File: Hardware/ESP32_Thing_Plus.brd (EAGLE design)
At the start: 33 x 58.9 mm, 52 parts, among them Q1 2.5A/30V, Q2 MBT3904DW1T1, U1 MCP73831, U2 ESP-WROOM-32, U3 AP2112K-3.3V, U4 FT231XS

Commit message: Ready for qc review
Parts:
- added FD3, FD4: FIDUCIALUFIDUCIAL, SparkFun-Aesthetics:MICRO-FIDUCIAL
- moved FD2 94.5 mm to (31.8, 57.1), flipped to the top
- moved J2 63.5 mm to (31.8, 1.27), flipped to the top
- moved LOGO1 57.4 mm to (28.7, 12.7), flipped to the top
- moved D4 55.9 mm to (27.9, 29.2), flipped to the top
- moved R8 55.9 mm to (27.9, 27.7), flipped to the top
- moved LOGO3 54.6 mm to (27.3, 53.1), flipped to the bottom
- moved J3 52.1 mm to (26.0, 5.08), flipped to the top
- moved R9 43.2 mm to (21.6, 24.1), flipped to the top
- moved C19 41.9 mm to (21.0, 11.4), flipped to the top
- moved C6 38.1 mm to (19.1, 8.51), flipped to the top
- moved JP2 38.1 mm to (19.1, 5.97), flipped to the top
- moved R17 38.1 mm to (19.1, 19.1), flipped to the top
- moved S2 38.1 mm to (19.1, 24.1), flipped to the top
- moved R5 36.8 mm to (18.4, 14.6), flipped to the top
- moved R6 36.8 mm to (18.4, 14.6), flipped to the top
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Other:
- board text added: "Mike Hord"
- board text added: "Original ESP32 Thing Design by Jim Lindblom"
- board text removed: "Jim Lindblom"

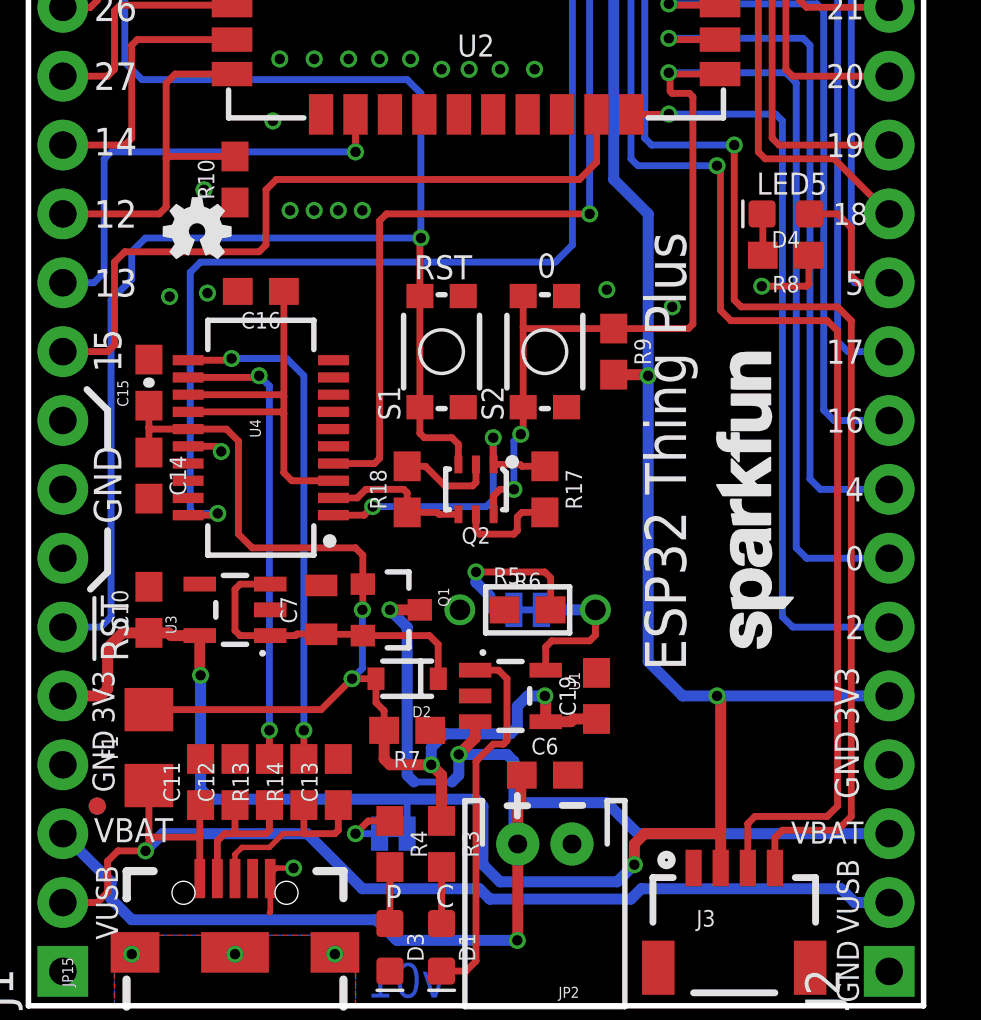
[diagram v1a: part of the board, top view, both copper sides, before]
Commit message: Revised per QC double check
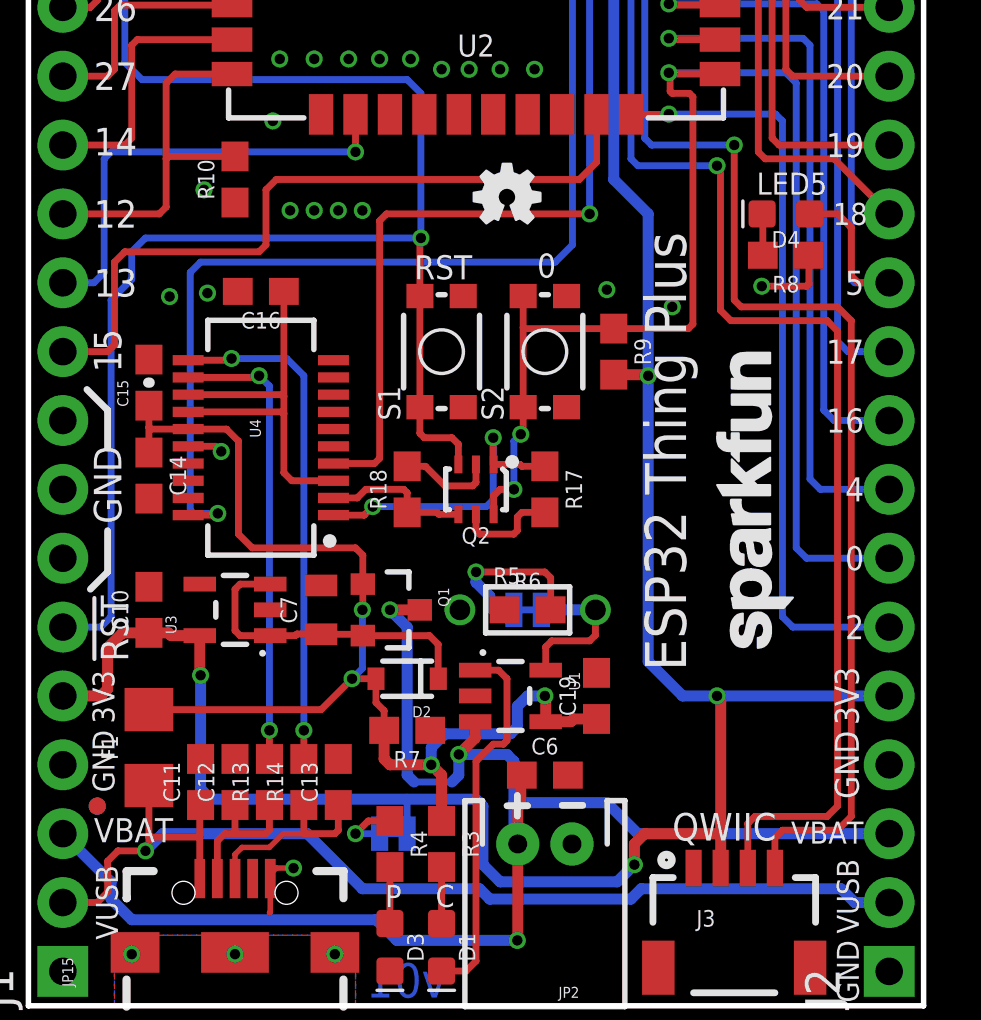
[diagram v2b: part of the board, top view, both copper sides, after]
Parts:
- moved LOGO2 11.5 mm to (17.7, 29.8)
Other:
- board text added: "Measurements in inches"
- board text added: "QWIIC"
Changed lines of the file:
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@@
 <layers>
 <layer number="1" name="Top" color="4" fill="1" visible="yes" active="yes"/>
-<layer number="2" name="Route2" color="1" fill="3" visible="no" active="yes"/>
-<layer number="15" name="Route15" color="4" fill="6" visible="no" active="yes"/>
+<layer number="2" name="Route2" color="1" fill="3" visible="yes" active="yes"/>
+<layer number="15" name="Route15" color="4" fill="6" visible="yes" active="yes"/>
 <layer number="16" name="Bottom" color="1" fill="1" visible="yes" active="yes"/>
 <layer number="17" name="Pads" color="2" fill="1" visible="yes" active="yes"/>
@@
 <layer number="23" name="tOrigins" color="15" fill="1" visible="yes" active="yes"/>
 <layer number="24" name="bOrigins" color="15" fill="1" visible="yes" active="yes"/>
-<layer number="25" name="tNames" color="7" fill="1" visible="no" active="yes"/>
-<layer number="26" name="bNames" color="7" fill="1" visible="no" active="yes"/>
-<layer number="27" name="tValues" color="7" fill="1" visible="no" active="yes"/>
-<layer number="28" name="bValues" color="7" fill="1" visible="no" active="yes"/>
-<layer number="29" name="tStop" color="7" fill="3" visible="no" active="yes"/>
-<layer number="30" name="bStop" color="7" fill="6" visible="no" active="yes"/>
-<layer number="31" name="tCream" color="7" fill="4" visible="no" active="yes"/>
-<layer number="32" name="bCream" color="7" fill="5" visible="no" active="yes"/>
-<layer number="39" name="tKeepout" color="4" fill="11" visible="no" active="yes"/>
-<layer number="40" name="bKeepout" color="1" fill="11" visible="no" active="yes"/>
-<layer number="41" name="tRestrict" color="4" fill="10" visible="no" active="yes"/>
-<layer number="42" name="bRestrict" color="1" fill="10" visible="no" active="yes"/>
-<layer number="43" name="vRestrict" color="2" fill="10" visible="no" active="yes"/>
-<layer number="44" name="Drills" color="7" fill="1" visible="no" active="yes"/>
+<layer number="25" name="tNames" color="7" fill="1" visible="yes" active="yes"/>
+<layer number="26" name="bNames" color="7" fill="1" visible="yes" active="yes"/>
+<layer number="27" name="tValues" color="7" fill="1" visible="yes" active="yes"/>
+<layer number="28" name="bValues" color="7" fill="1" visible="yes" active="yes"/>
+<layer number="29" name="tStop" color="7" fill="3" visible="yes" active="yes"/>
+<layer number="30" name="bStop" color="7" fill="6" visible="yes" active="yes"/>
+<layer number="31" name="tCream" color="7" fill="4" visible="yes" active="yes"/>
+<layer number="32" name="bCream" color="7" fill="5" visible="yes" active="yes"/>
+<layer number="39" name="tKeepout" color="4" fill="11" visible="yes" active="yes"/>
+<layer number="40" name="bKeepout" color="1" fill="11" visible="yes" active="yes"/>
+<layer number="41" name="tRestrict" color="4" fill="10" visible="yes" active="yes"/>
+<layer number="42" name="bRestrict" color="1" fill="10" visible="yes" active="yes"/>
+<layer number="43" name="vRestrict" color="2" fill="10" visible="yes" active="yes"/>
+<layer number="44" name="Drills" color="7" fill="1" visible="yes" active="yes"/>
 <layer number="45" name="Holes" color="7" fill="1" visible="yes" active="yes"/>
-<layer number="46" name="Milling" color="3" fill="1" visible="no" active="yes"/>
-<layer number="47" name="Measures" color="7" fill="1" visible="no" active="yes"/>
-<layer number="48" name="Document" color="7" fill="1" visible="no" active="yes"/>
-<layer number="49" name="Reference" color="7" fill="1" visible="no" active="yes"/>
+<layer number="46" name="Milling" color="3" fill="1" visible="yes" active="yes"/>
+<layer number="47" name="Measures" color="7" fill="1" visible="yes" active="yes"/>
+<layer number="48" name="Document" color="7" fill="1" visible="yes" active="yes"/>
+<layer number="49" name="Reference" color="7" fill="1" visible="yes" active="yes"/>
 <layer number="51" name="tDocu" color="6" fill="1" visible="yes" active="yes"/>
-<layer number="52" name="bDocu" color="7" fill="1" visible="no" active="yes"/>
+<layer number="52" name="bDocu" color="7" fill="1" visible="yes" active="yes"/>
 <layer number="3" name="Route3" color="4" fill="3" visible="no" active="no"/>
 <layer number="4" name="Route4" color="1" fill="4" visible="no" active="no"/>
@@
 <layer number="59" name="tCarbon" color="7" fill="1" visible="no" active="no"/>
 <layer number="60" name="bCarbon" color="7" fill="1" visible="no" active="no"/>
-<layer number="88" name="SimResults" color="9" fill="1" visible="no" active="yes"/>
-<layer number="89" name="SimProbes" color="9" fill="1" visible="no" active="yes"/>
+<layer number="88" name="SimResults" color="9" fill="1" visible="yes" active="yes"/>
+<layer number="89" name="SimProbes" color="9" fill="1" visible="yes" active="yes"/>
 <layer number="90" name="Modules" color="5" fill="1" visible="no" active="no"/>
 <layer number="91" name="Nets" color="2" fill="1" visible="no" active="no"/>
@@
 <dimension x1="0" y1="0" x2="33.02" y2="0" x3="16.51" y3="-10.16" textsize="1.778" textratio="15" layer="47" dtype="horizontal" unit="inch"/>
 <circle x="6.223" y="52.197" radius="0.179603125" width="0.4064" layer="21"/>
+<text x="43.18" y="16.51" size="1.778" layer="47" font="vector" ratio="15">Measurements in inches</text>
+<text x="23.749" y="6.096" size="1.016" layer="21" font="vector" ratio="15">QWIIC</text>
 </plain>
 <attributes>
@@
 <attribute name="PROD_ID" value="RES-00818" x="27.94" y="27.686" size="1.778" layer="27" font="vector" ratio="15" rot="R180" display="off"/>
 </element>
-<element name="LOGO2" library="SparkFun-Aesthetics" package="OSHW-LOGO-MINI" value="OSHW-LOGOMINI" x="6.223" y="28.575"/>
+<element name="LOGO2" library="SparkFun-Aesthetics" package="OSHW-LOGO-MINI" value="OSHW-LOGOMINI" x="17.653" y="29.845"/>
 <element name="FD1" library="SparkFun-Aesthetics" package="MICRO-FIDUCIAL" value="FIDUCIALUFIDUCIAL" x="2.54" y="7.366"/>
 <element name="FD2" library="SparkFun-Aesthetics" package="MICRO-FIDUCIAL" value="FIDUCIALUFIDUCIAL" x="31.75" y="57.15"/>

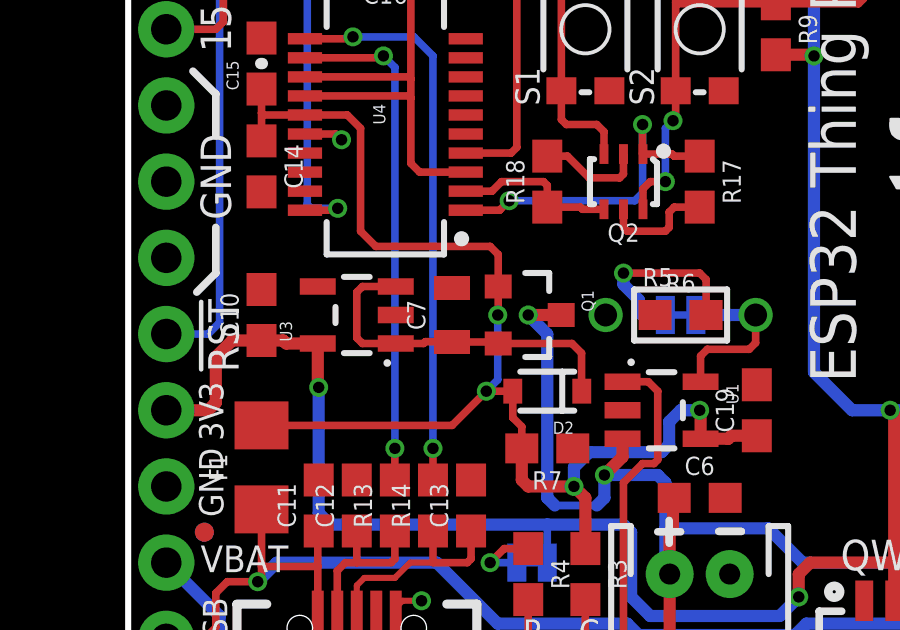
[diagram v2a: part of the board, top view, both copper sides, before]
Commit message: Replaced EOL 1.0uF cap with newer one
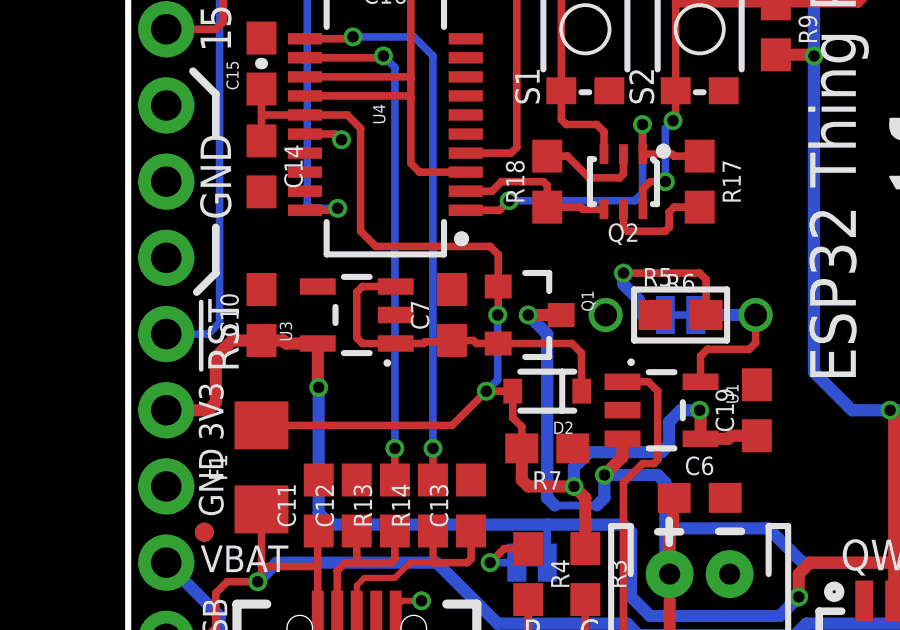
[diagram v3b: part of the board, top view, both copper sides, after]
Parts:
- C7: device SparkFun-Capacitors:0805 -> SparkFun-Capacitors:0603
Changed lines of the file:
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@@
 <layers>
 <layer number="1" name="Top" color="4" fill="1" visible="yes" active="yes"/>
-<layer number="2" name="Route2" color="1" fill="3" visible="yes" active="yes"/>
-<layer number="15" name="Route15" color="4" fill="6" visible="yes" active="yes"/>
+<layer number="2" name="Route2" color="1" fill="3" visible="no" active="yes"/>
+<layer number="15" name="Route15" color="4" fill="6" visible="no" active="yes"/>
 <layer number="16" name="Bottom" color="1" fill="1" visible="yes" active="yes"/>
 <layer number="17" name="Pads" color="2" fill="1" visible="yes" active="yes"/>
@@
 <layer number="23" name="tOrigins" color="15" fill="1" visible="yes" active="yes"/>
 <layer number="24" name="bOrigins" color="15" fill="1" visible="yes" active="yes"/>
-<layer number="25" name="tNames" color="7" fill="1" visible="yes" active="yes"/>
-<layer number="26" name="bNames" color="7" fill="1" visible="yes" active="yes"/>
-<layer number="27" name="tValues" color="7" fill="1" visible="yes" active="yes"/>
-<layer number="28" name="bValues" color="7" fill="1" visible="yes" active="yes"/>
-<layer number="29" name="tStop" color="7" fill="3" visible="yes" active="yes"/>
-<layer number="30" name="bStop" color="7" fill="6" visible="yes" active="yes"/>
-<layer number="31" name="tCream" color="7" fill="4" visible="yes" active="yes"/>
-<layer number="32" name="bCream" color="7" fill="5" visible="yes" active="yes"/>
-<layer number="39" name="tKeepout" color="4" fill="11" visible="yes" active="yes"/>
-<layer number="40" name="bKeepout" color="1" fill="11" visible="yes" active="yes"/>
-<layer number="41" name="tRestrict" color="4" fill="10" visible="yes" active="yes"/>
-<layer number="42" name="bRestrict" color="1" fill="10" visible="yes" active="yes"/>
-<layer number="43" name="vRestrict" color="2" fill="10" visible="yes" active="yes"/>
-<layer number="44" name="Drills" color="7" fill="1" visible="yes" active="yes"/>
+<layer number="25" name="tNames" color="7" fill="1" visible="no" active="yes"/>
+<layer number="26" name="bNames" color="7" fill="1" visible="no" active="yes"/>
+<layer number="27" name="tValues" color="7" fill="1" visible="no" active="yes"/>
+<layer number="28" name="bValues" color="7" fill="1" visible="no" active="yes"/>
+<layer number="29" name="tStop" color="7" fill="3" visible="no" active="yes"/>
+<layer number="30" name="bStop" color="7" fill="6" visible="no" active="yes"/>
+<layer number="31" name="tCream" color="7" fill="4" visible="no" active="yes"/>
+<layer number="32" name="bCream" color="7" fill="5" visible="no" active="yes"/>
+<layer number="39" name="tKeepout" color="4" fill="11" visible="no" active="yes"/>
+<layer number="40" name="bKeepout" color="1" fill="11" visible="no" active="yes"/>
+<layer number="41" name="tRestrict" color="4" fill="10" visible="no" active="yes"/>
+<layer number="42" name="bRestrict" color="1" fill="10" visible="no" active="yes"/>
+<layer number="43" name="vRestrict" color="2" fill="10" visible="no" active="yes"/>
+<layer number="44" name="Drills" color="7" fill="1" visible="no" active="yes"/>
 <layer number="45" name="Holes" color="7" fill="1" visible="yes" active="yes"/>
-<layer number="46" name="Milling" color="3" fill="1" visible="yes" active="yes"/>
-<layer number="47" name="Measures" color="7" fill="1" visible="yes" active="yes"/>
-<layer number="48" name="Document" color="7" fill="1" visible="yes" active="yes"/>
-<layer number="49" name="Reference" color="7" fill="1" visible="yes" active="yes"/>
+<layer number="46" name="Milling" color="3" fill="1" visible="no" active="yes"/>
+<layer number="47" name="Measures" color="7" fill="1" visible="no" active="yes"/>
+<layer number="48" name="Document" color="7" fill="1" visible="no" active="yes"/>
+<layer number="49" name="Reference" color="7" fill="1" visible="no" active="yes"/>
 <layer number="51" name="tDocu" color="6" fill="1" visible="yes" active="yes"/>
-<layer number="52" name="bDocu" color="7" fill="1" visible="yes" active="yes"/>
+<layer number="52" name="bDocu" color="7" fill="1" visible="no" active="yes"/>
 <layer number="3" name="Route3" color="4" fill="3" visible="no" active="no"/>
 <layer number="4" name="Route4" color="1" fill="4" visible="no" active="no"/>
@@
 <layer number="59" name="tCarbon" color="7" fill="1" visible="no" active="no"/>
 <layer number="60" name="bCarbon" color="7" fill="1" visible="no" active="no"/>
-<layer number="88" name="SimResults" color="9" fill="1" visible="yes" active="yes"/>
-<layer number="89" name="SimProbes" color="9" fill="1" visible="yes" active="yes"/>
+<layer number="88" name="SimResults" color="9" fill="1" visible="no" active="yes"/>
+<layer number="89" name="SimProbes" color="9" fill="1" visible="no" active="yes"/>
 <layer number="90" name="Modules" color="5" fill="1" visible="no" active="no"/>
 <layer number="91" name="Nets" color="2" fill="1" visible="no" active="no"/>
@@
 <attribute name="PROD_ID" value="CAP-08280" x="15.875" y="14.097" size="1.778" layer="27" font="vector" ratio="15" rot="R90" display="off"/>
 </element>
-<element name="C7" library="SparkFun-Capacitors" package="0805" value="1.0uF" x="10.795" y="14.605" rot="R90">
-<attribute name="PROD_ID" value="CAP-11625" x="28.575" y="0.635" size="1.778" layer="27" font="vector" ratio="15" rot="R90" display="off"/>
+<element name="C7" library="SparkFun-Capacitors" package="0603" value="1.0uF" x="10.795" y="14.605" rot="R90">
+<attribute name="PROD_ID" value="CAP-13930" x="28.575" y="0.635" size="1.778" layer="27" font="vector" ratio="15" rot="R90" display="off"/>
 </element>
 <element name="C10" library="SparkFun-Capacitors" package="0603" value="2.2uF" x="4.445" y="14.605" rot="R90">
@@
 <wire x1="9.845" y1="13.655" x2="9.906" y2="13.716" width="0.254" layer="1"/>
 <wire x1="9.906" y1="13.716" x2="10.784" y2="13.716" width="0.254" layer="1"/>
-<wire x1="10.784" y1="13.716" x2="10.795" y2="13.705" width="0.254" layer="1"/>
-<wire x1="10.795" y1="13.705" x2="12.285" y2="13.705" width="0.254" layer="1"/>
-<wire x1="12.285" y1="13.705" x2="12.335" y2="13.655" width="0.254" layer="1"/>
 <wire x1="8.9201" y1="13.655" x2="7.808" y2="13.655" width="0.254" layer="1"/>
 <wire x1="7.808" y1="13.655" x2="7.62" y2="13.843" width="0.254" layer="1"/>
@@
 <wire x1="8.9201" y1="15.555" x2="7.808" y2="15.555" width="0.254" layer="1"/>
 <wire x1="7.808" y1="15.555" x2="7.62" y2="15.367" width="0.254" layer="1"/>
+<wire x1="12.335" y1="13.655" x2="11.618" y2="13.655" width="0.254" layer="1"/>
+<wire x1="11.618" y1="13.655" x2="11.518" y2="13.755" width="0.254" layer="1"/>
+<wire x1="10.795" y1="13.755" x2="11.518" y2="13.755" width="0.254" layer="1"/>
+<wire x1="10.795" y1="13.755" x2="10.795" y2="13.727" width="0.254" layer="1"/>
+<wire x1="10.795" y1="13.727" x2="10.784" y2="13.716" width="0.254" layer="1"/>
 </signal>
 <signal name="RTS">
